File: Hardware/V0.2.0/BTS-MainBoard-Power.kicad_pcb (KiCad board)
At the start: 4 copper layers, 83 x 86.5 mm, 87 parts, among them J10 PeCon, J11 PeCon, J12 FanConn, J13 FanConn, J14 FanConn, J15 FanConn, J16 FanConn, J17 FanConn, J18 FanConn, J19 FanConn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

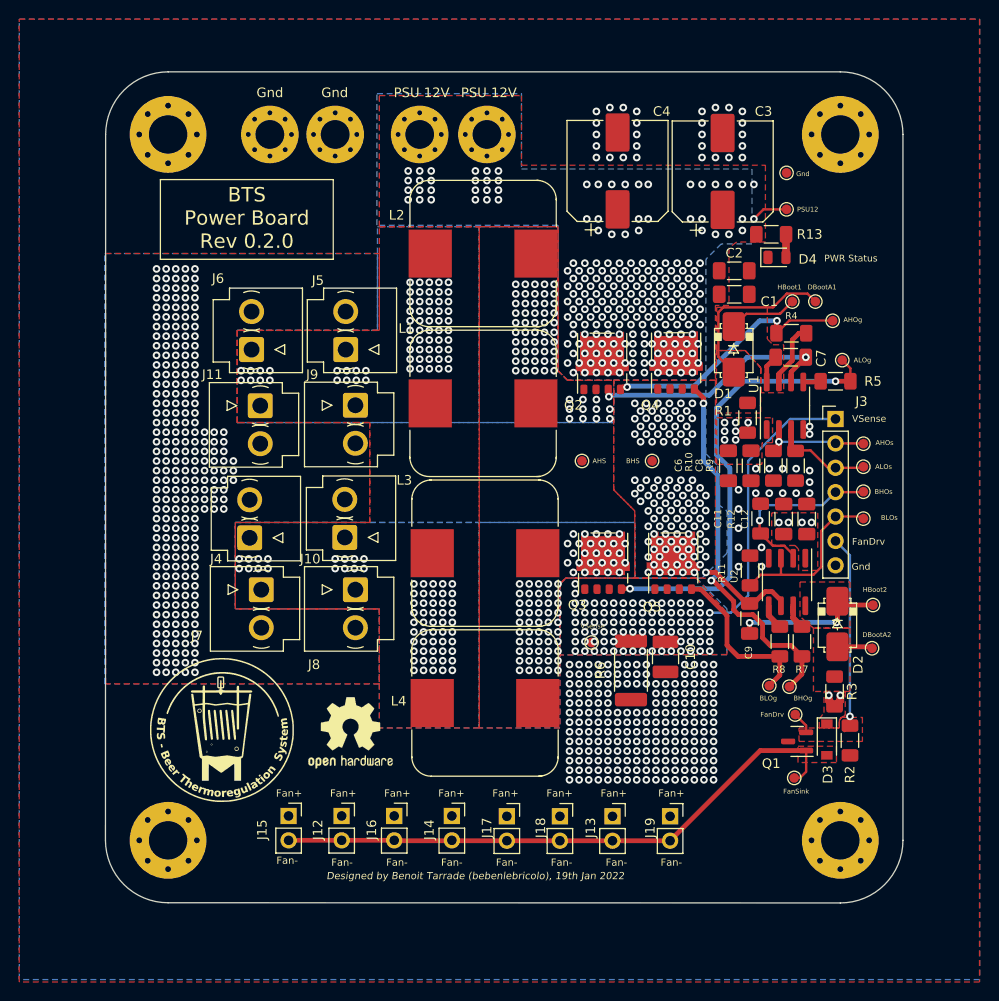
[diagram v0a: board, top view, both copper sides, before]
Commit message: Reduced vias count, there were too many in there
Signed-off-by: bebenlebricolo <benoittarrade@hotmail.fr>
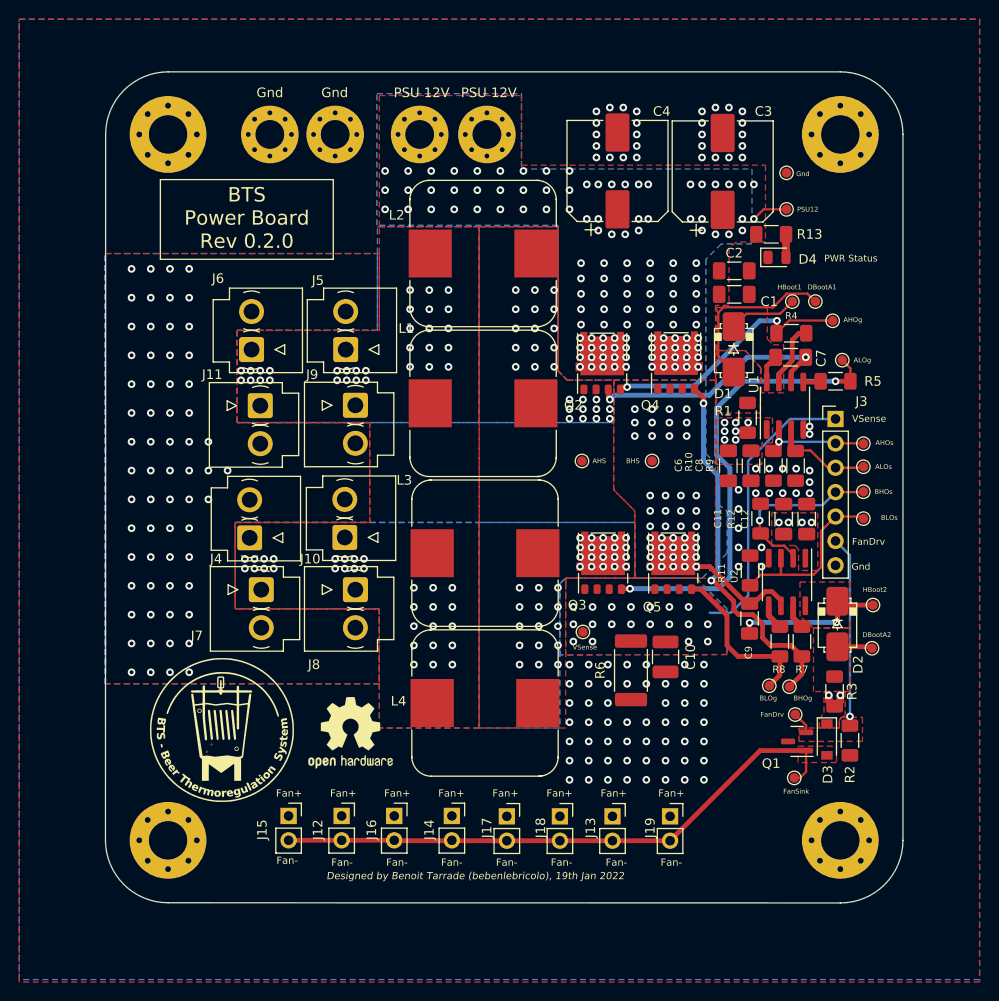
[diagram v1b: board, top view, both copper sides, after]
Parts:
- moved TP19 1.42 mm to (157.2, 100.8)
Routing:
- net /BHS: track 10.6 -> 11.9 mm, vias 352 -> 108
- net /AHS: track 26.2 -> 26.6 mm, vias 140 -> 63
- net GND: vias 242 -> 101
- net /VSense: vias 85 -> 19
- net /Psu12V: vias 232 -> 138
- net /HBridge/+Peltier: vias 132 -> 62

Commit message: Moved Libraries and improved graphics
Signed-off-by: bebenlebricolo <benoittarrade@hotmail.fr>
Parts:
- added G***: LOGO, BTS-MainBoard-Power-Labels:ALOs_label, F.Cu at (188.0, 83.8)
- added G***: LOGO, BTS-MainBoard-Power-Labels:BHOs_label, F.Cu at (188.0, 86.4)
- added G***: LOGO, BTS-MainBoard-Power-Labels:GND_label, F.Cu at (188.0, 94.2)
- added G***: LOGO, BTS-MainBoard-Power-Labels:FanDrive_label, F.Cu at (188.0, 91.6)
- added G***: LOGO, BTS-MainBoard-Power-Labels:BLOs_label, F.Cu at (188.0, 89.0)
- added G***: LOGO, BTS-MainBoard-Power-Labels:BoardMainLabel, F.Cu at (125.6, 57.2)
- added G***: LOGO, BTS-MainBoard-Power-Labels:AHOs_label, F.Cu at (188.0, 81.2)
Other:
- board text removed: "AHOs"
- board text removed: "ALOs"
- board text removed: "BHOs"
- board text removed: "BLOs"
- board text removed: "BTS Power Board Rev 0.2.0"
